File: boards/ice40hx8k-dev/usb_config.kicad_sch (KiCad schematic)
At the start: 2 parts, among them U1 ICE40HX8K-CT256

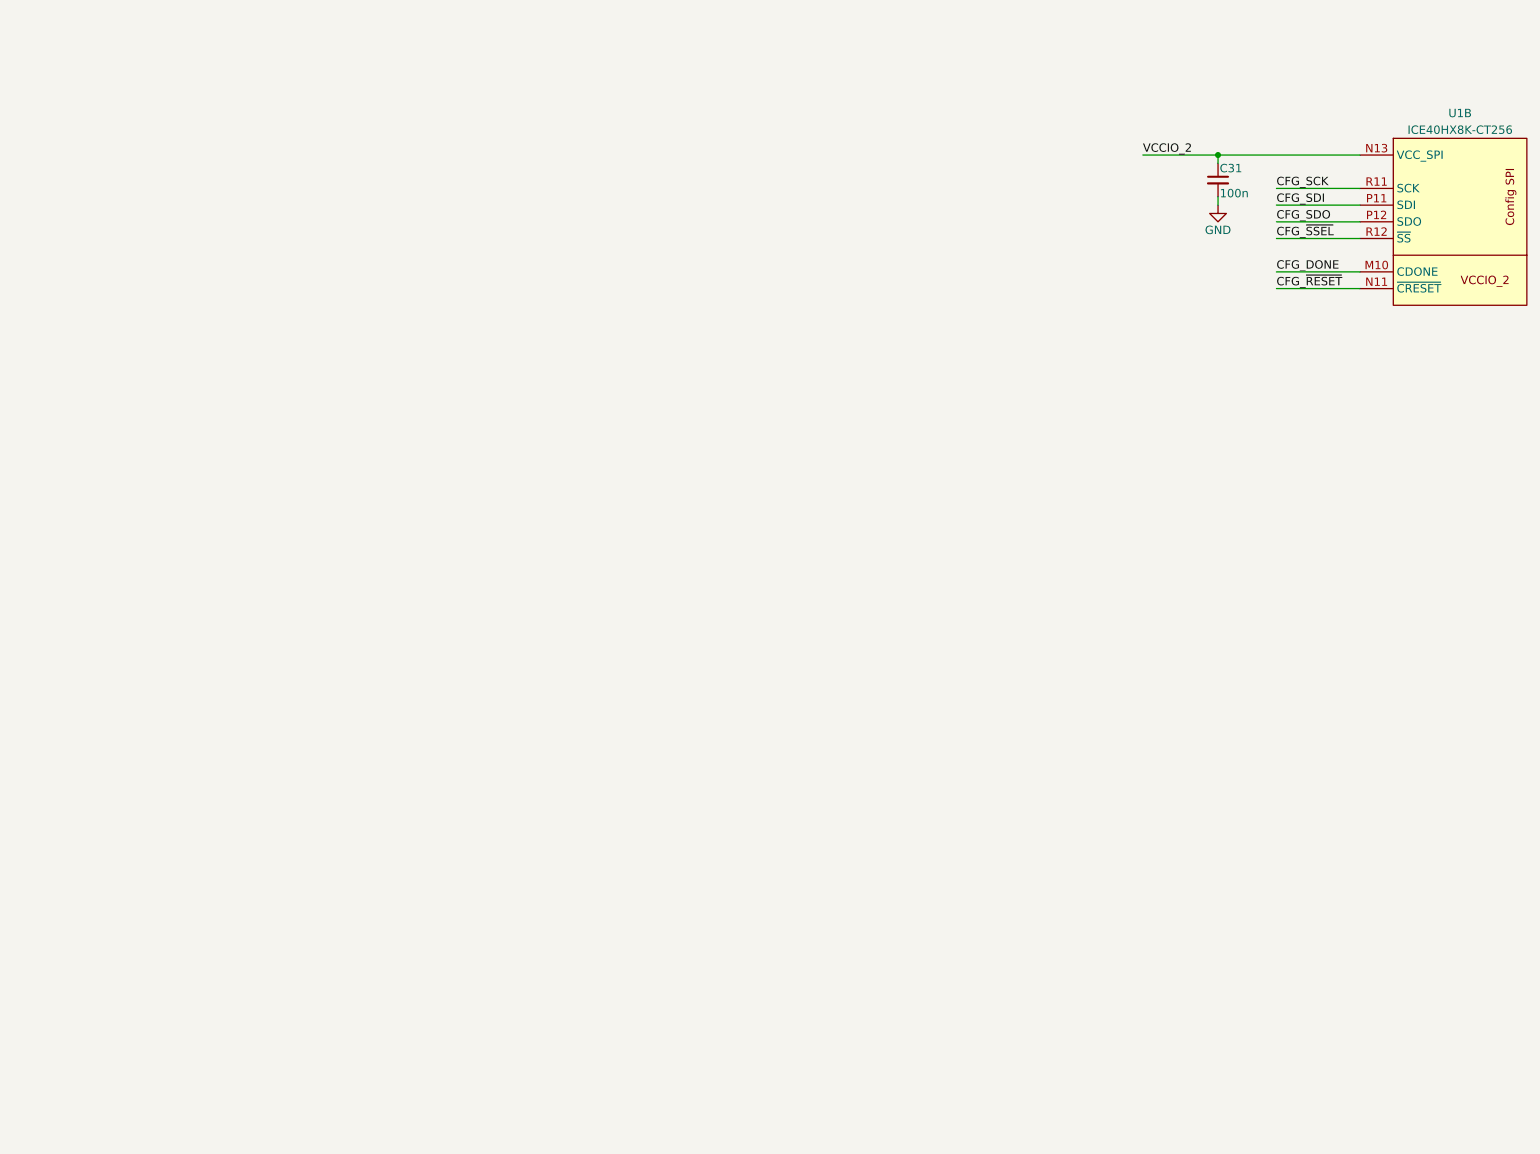
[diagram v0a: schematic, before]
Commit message: Add USB connector and FT2323 symbol.
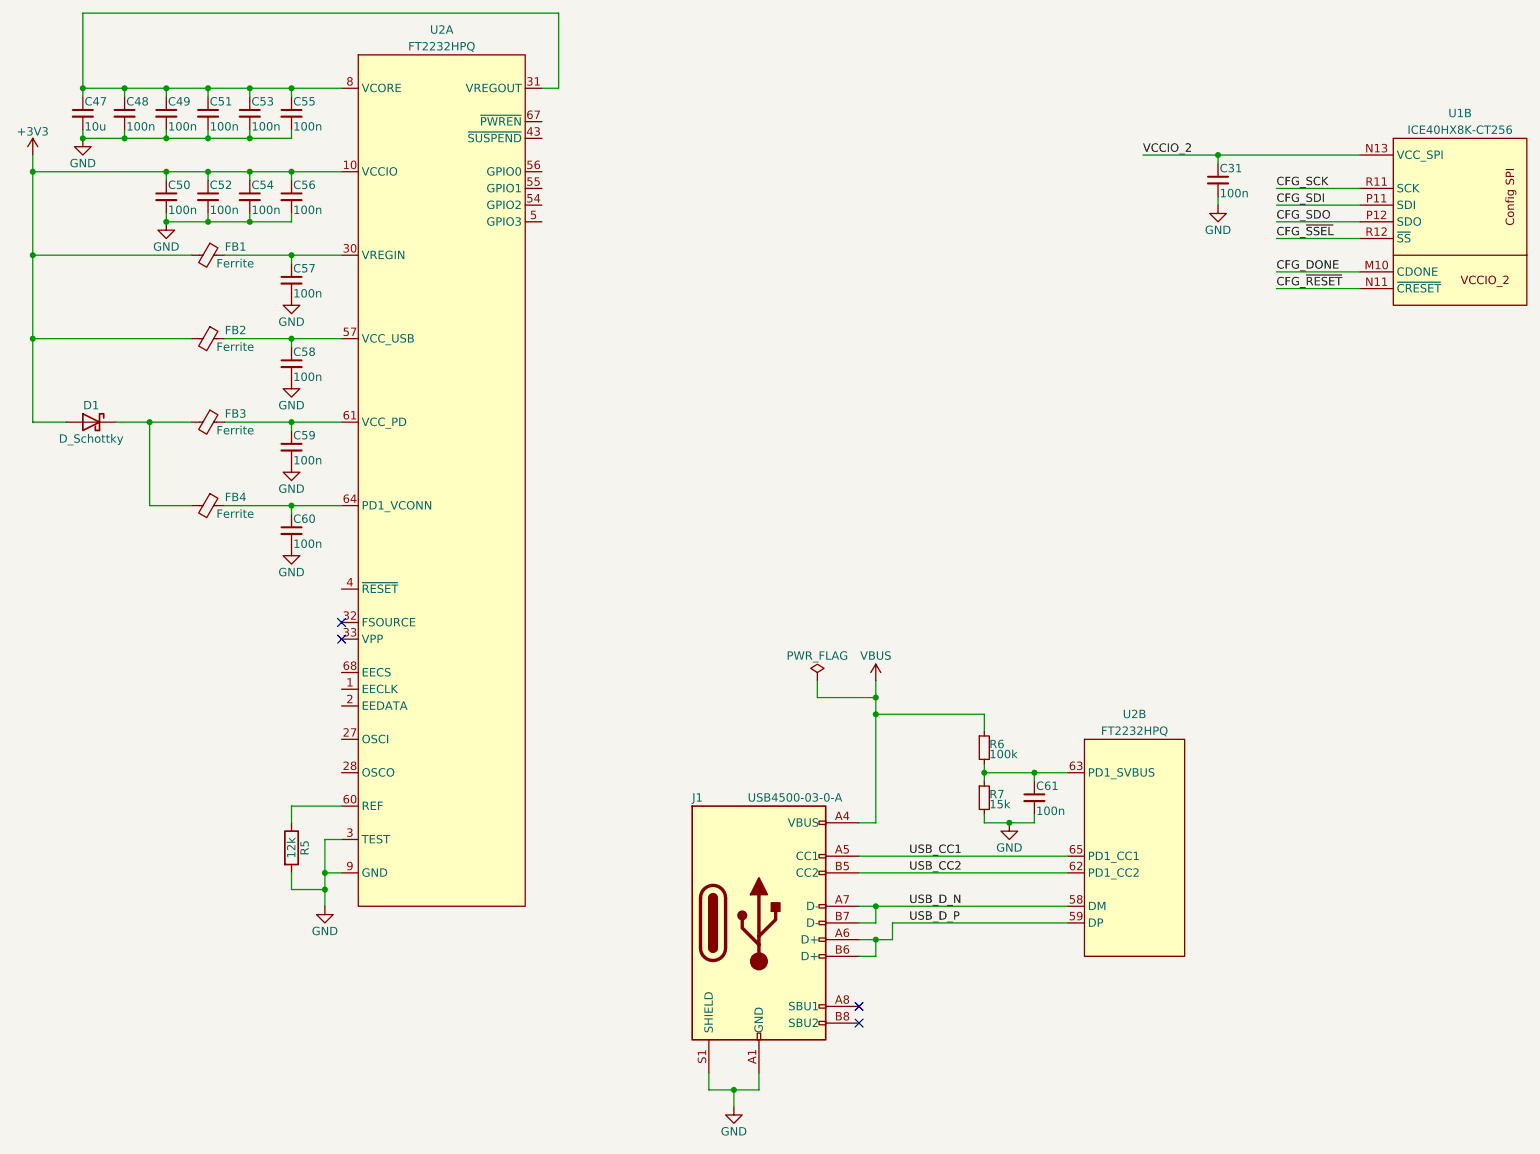
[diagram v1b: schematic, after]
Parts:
- added C47: 10u, 0Local:C_SMD_0402_Pad0.5mm, symbol Device:C_Small
- added C48, C49, C50, C51, C52, C53, C54, C55, C56, C57, C58, C59, C60, C61: 100n, 0Local:C_SMD_0402_Pad0.5mm, symbol Device:C_Small
- added D1: D_Schottky, Diode_SMD:D_0603_1608Metric, symbol Device:D_Schottky
- added FB1, FB2, FB3, FB4: Ferrite, symbol Device:FerriteBead_Small
- added J1: USB4500-03-0-A, 0Local:GCT_USB4500, symbol Connector:USB_C_Receptacle_USB2.0
- added R5: 12k, Resistor_SMD:R_0603_1608Metric, symbol Device:R
- added R6: 100k, symbol Device:R_Small
- added R7: 15k, symbol Device:R_Small
- added U2: FT2232HPQ, Package_DFN_QFN:QFN-68-1EP_8x8mm_P0.4mm_EP5.2x5.2mm, symbol 0Local:FT2232HPQ
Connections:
- net GND: now also C47.2, C48.2, C49.2, C50.2, C51.2, C52.2, C53.2, C54.2, C55.2, C56.2, C57.2, C58.2, C59.2, C60.2, C61.2, J1.A1 (GND), J1.A12 (GND), J1.B1 (GND), J1.B12 (GND), J1.S1 (SHIELD), R5.2, R7.2, U2.29 (GND), U2.3 (TEST), U2.9 (GND)
- new net: C58.1, FB2.1, U2.57 (VCC_USB)
- new net: C47.1, C48.1, C49.1, C51.1, C53.1, C55.1, U2.25 (VCORE), U2.31 (VREGOUT), U2.44 (VCORE), U2.66 (VCORE), U2.8 (VCORE)
- new net: C61.1, R6.2, R7.1, U2.63 (PD1_SVBUS)
- new net: C57.1, FB1.1, U2.30 (VREGIN)
- new net: R5.1, U2.60 (REF)
- new net: C60.1, FB4.1, U2.64 (PD1_VCONN)
- new net: D1.1 (K), FB3.2, FB4.2
- new net: C59.1, FB3.1, U2.61 (VCC_PD)
- new net +3V3: C50.1, C52.1, C54.1, C56.1, D1.2 (A), FB1.2, FB2.2, U2.10 (VCCIO), U2.26 (VCCIO), U2.39 (VCCIO), U2.51 (VCCIO)
- new net USB_CC1: J1.A5 (CC1), U2.65 (PD1_CC1)
- new net USB_CC2: J1.B5 (CC2), U2.62 (PD1_CC2)
- new net USB_D_N: J1.A7 (D-), J1.B7 (D-), U2.58 (DM)
- new net USB_D_P: J1.A6 (D+), J1.B6 (D+), U2.59 (DP)
- new net VBUS: J1.A4 (VBUS), J1.A9 (VBUS), J1.B4 (VBUS), J1.B9 (VBUS), R6.1
- no-connect marks 0 -> 4

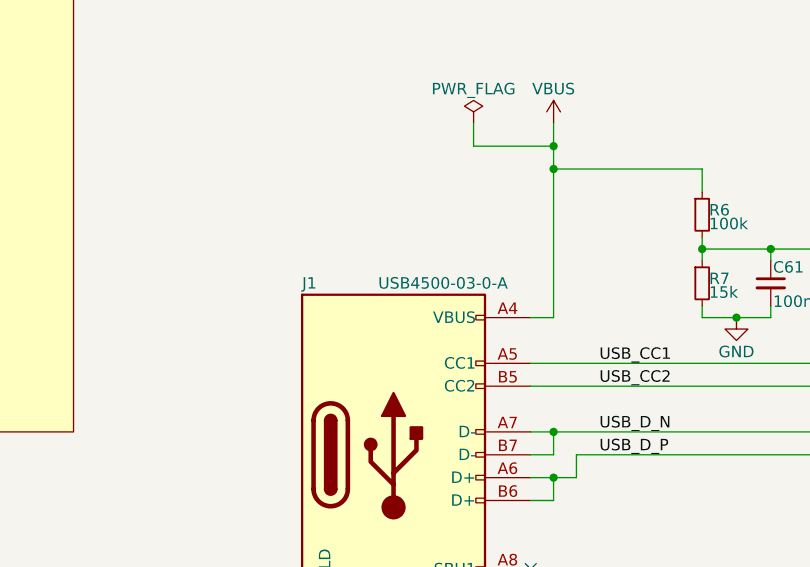
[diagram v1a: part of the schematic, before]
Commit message: Use a lower-profile version of the USB connector.
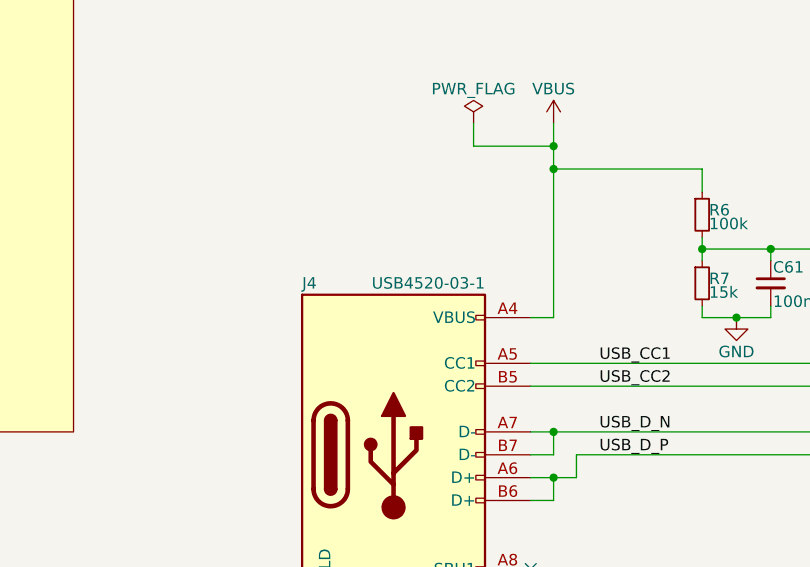
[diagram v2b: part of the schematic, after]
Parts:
- J4: renamed from J1; value USB4500-03-0-A -> USB4520-03-1; footprint 0Local:GCT_USB4500 -> 0Local:GCT_USB45xx
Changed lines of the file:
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@@
   (symbol (lib_id "Connector:USB_C_Receptacle_USB2.0") (at 137.16 157.48 0) (unit 1)
     (in_bom yes) (on_board yes)
-    (property "Reference" "J1" (id 0) (at 127 138.43 0)
+    (property "Reference" "J4" (id 0) (at 127 138.43 0)
       (effects (font (size 1.27 1.27)) (justify left))
     )
-    (property "Value" "USB4500-03-0-A" (id 1) (at 149.86 138.43 0)
+    (property "Value" "USB4520-03-1" (id 1) (at 147.32 138.43 0)
       (effects (font (size 1.27 1.27)) (justify right))
     )
-    (property "Footprint" "0Local:GCT_USB4500" (id 2) (at 140.97 157.48 0)
+    (property "Footprint" "0Local:GCT_USB45xx" (id 2) (at 140.97 157.48 0)
       (effects (font (size 1.27 1.27)) hide)
     )
-    (property "Datasheet" "https://www.usb.org/sites/default/files/documents/usb_type-c.zip" (id 3) (at 140.97 157.48 0)
+    (property "Datasheet" "https://gct.co/files/drawings/usb4520.pdf" (id 3) (at 140.97 157.48 0)
       (effects (font (size 1.27 1.27)) hide)
     )

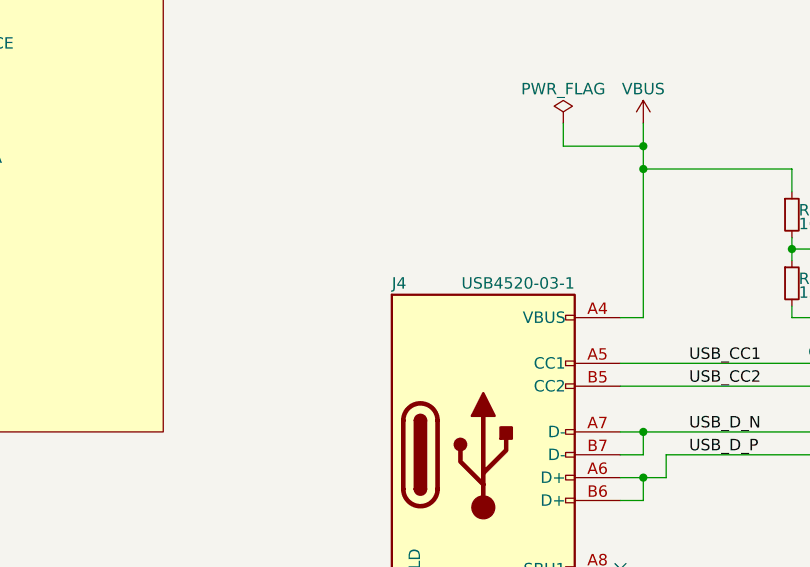
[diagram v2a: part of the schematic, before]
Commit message: Add Hirose connectors and standoffs.
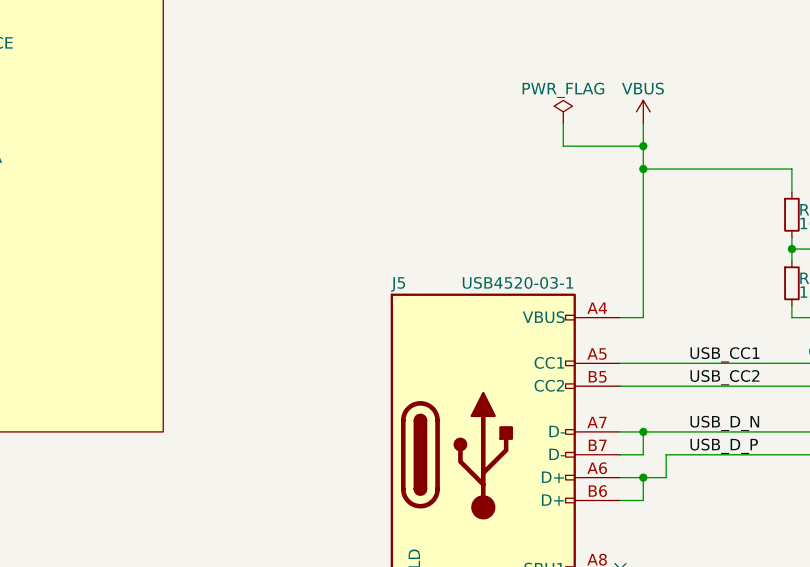
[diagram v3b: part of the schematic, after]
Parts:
- R6, R7: footprint (none) -> Resistor_SMD:R_0603_1608Metric
- renumbered J4 to J5
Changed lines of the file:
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@@
       (effects (font (size 1.27 1.27)) (justify left))
     )
-    (property "Footprint" "" (id 2) (at 171.45 138.43 0)
+    (property "Footprint" "Resistor_SMD:R_0603_1608Metric" (id 2) (at 171.45 138.43 0)
       (effects (font (size 1.27 1.27)) hide)
     )
@@
   (symbol (lib_id "Connector:USB_C_Receptacle_USB2.0") (at 137.16 157.48 0) (unit 1)
     (in_bom yes) (on_board yes)
-    (property "Reference" "J4" (id 0) (at 127 138.43 0)
+    (property "Reference" "J5" (id 0) (at 127 138.43 0)
       (effects (font (size 1.27 1.27)) (justify left))
     )
@@
       (effects (font (size 1.27 1.27)) (justify left))
     )
-    (property "Footprint" "" (id 2) (at 171.45 130.81 0)
-      (effects (font (size 1.27 1.27)) hide)
-    )
+    (property "Footprint" "Resistor_SMD:R_0603_1608Metric" (id 2) (at 171.45 130.81 0)
+      (effects (font (size 1.27 1.27)) hide)
+    )
